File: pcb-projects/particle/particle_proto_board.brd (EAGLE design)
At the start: 60 x 57.8 mm, 37 parts, among them IC1 ATTINY20-SOIC-14S1, IC2 DMC2400UV-SOT563, IC3 DMC2400UV-SOT563

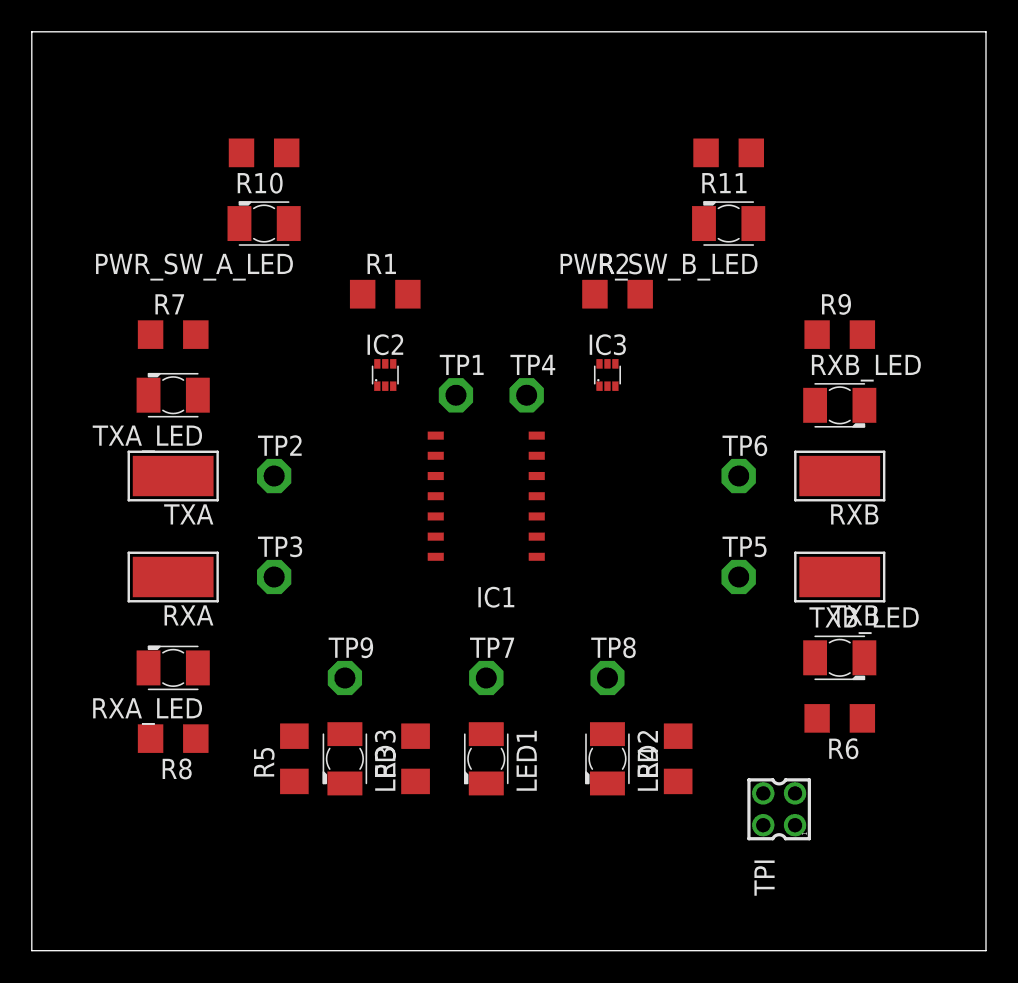
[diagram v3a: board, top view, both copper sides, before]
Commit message: routed bard
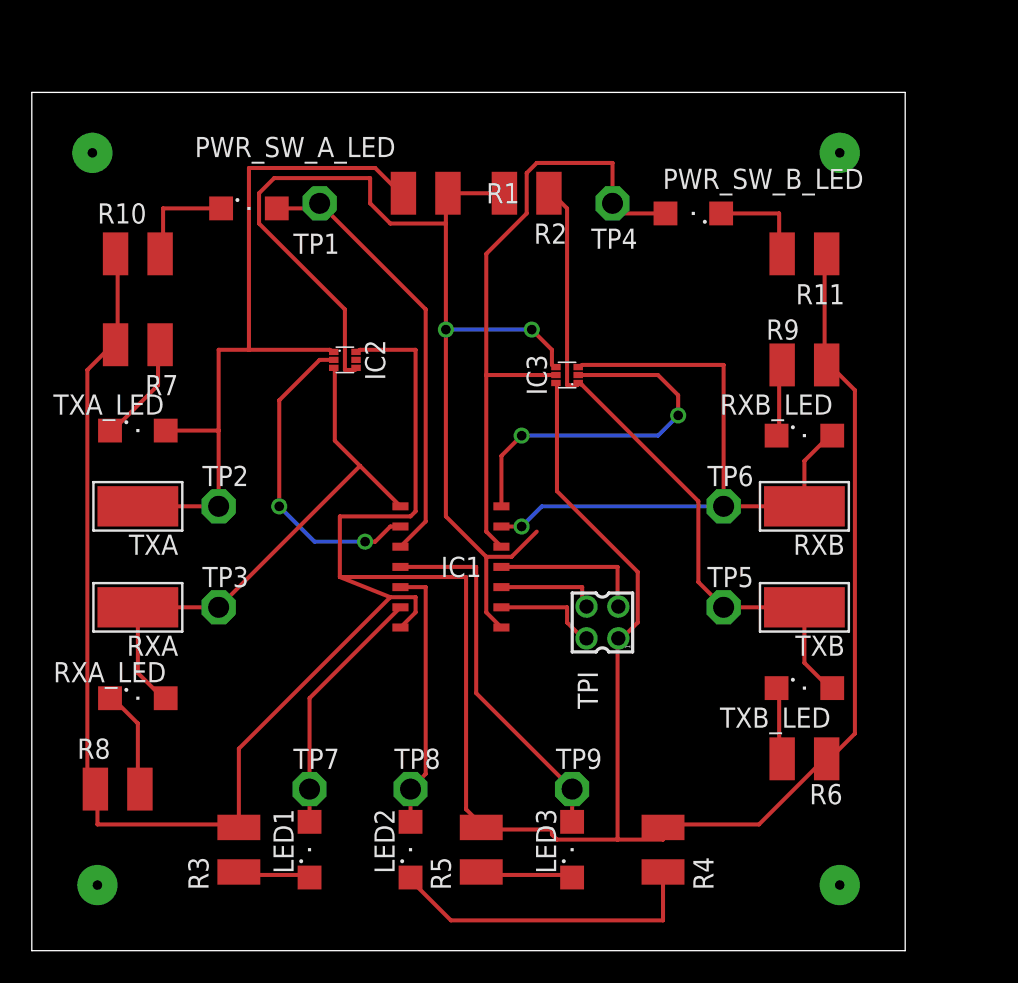
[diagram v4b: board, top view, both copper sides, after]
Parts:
- LED1, LED2, LED3, PWR_SW_A_LED, PWR_SW_B_LED, RXA_LED, RXB_LED, TXA_LED, TXB_LED: device led:KA-3528ASYC -> led:SML1206
- R1, R10, R11, R2, R3, R4, R5, R6, R7, R8, R9: device rcl:R1206 -> rcl:R1210
- moved TPI 16.2 mm to (35.9, 20.6)
- moved TP9 15.9 mm to (34.0, 10.2)
- moved LED3 15.4 mm to (34.0, 6.35), turned to 90 degrees
- moved TP1 14.8 mm to (18.1, 47.0)
- moved TP8 14.2 mm to (23.8, 10.2)
- moved LED2 13.6 mm to (23.8, 6.35), turned to 90 degrees
- moved TP4 13.2 mm to (36.5, 47.0)
- moved TP7 13.1 mm to (17.5, 10.2)
- moved R5 13.1 mm to (28.3, 6.35)
- moved LED1 12.5 mm to (17.5, 6.35), turned to 90 degrees
- moved R3 12.5 mm to (13.0, 6.35)
- moved R10 10.2 mm to (6.67, 43.8), turned to 0 degrees
- moved R2 8.54 mm to (31.1, 47.6), turned to 180 degrees
- moved R11 7.94 mm to (48.6, 43.8)
- moved R1 6.84 mm to (24.8, 47.6)
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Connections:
- net PWR_RX_SW_A: now also IC1.10; no longer IC1.8
- net PWR_RX_SW_B: now also IC1.5; no longer IC1.7
- net PWR_TX_A: now also IC1.9; no longer IC1.10
- net PWR_TX_B: now also IC1.7; no longer IC1.6
- net RX_A: now also IC1.8; no longer IC1.9
- net RX_B: now also IC1.6; no longer IC1.5
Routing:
- net GND: track 0.00 -> 208.9 mm, vias 0 -> 4
- net +5V: track 0.00 -> 73.1 mm, vias 0 -> 2
- net PWR_TX_A_A_A: track 0.00 -> 47.3 mm
- net RX_B: track 0.00 -> 42.9 mm, vias 0 -> 1
- net TXB: track 0.00 -> 42.4 mm
- net PWR_RX_SW_B: track 0.00 -> 41.5 mm
- net RX_A: track 0.00 -> 34.6 mm
- net PWR_RX_SW_A: track 0.00 -> 28.0 mm
- net PWR_TX_B: track 0.00 -> 23.4 mm, vias 0 -> 2
- net N$2: track 0.00 -> 23.3 mm
- net N$6: track 0.00 -> 20.1 mm
- net PWR_TX_A: track 0.00 -> 20.1 mm, vias 0 -> 2
- net N$3: track 0.00 -> 16.7 mm
- net N$1: track 0.00 -> 15.9 mm
- net RESET: track 0.00 -> 9.80 mm
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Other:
- board size 60 x 57.8 mm -> 54.9 x 54 mm

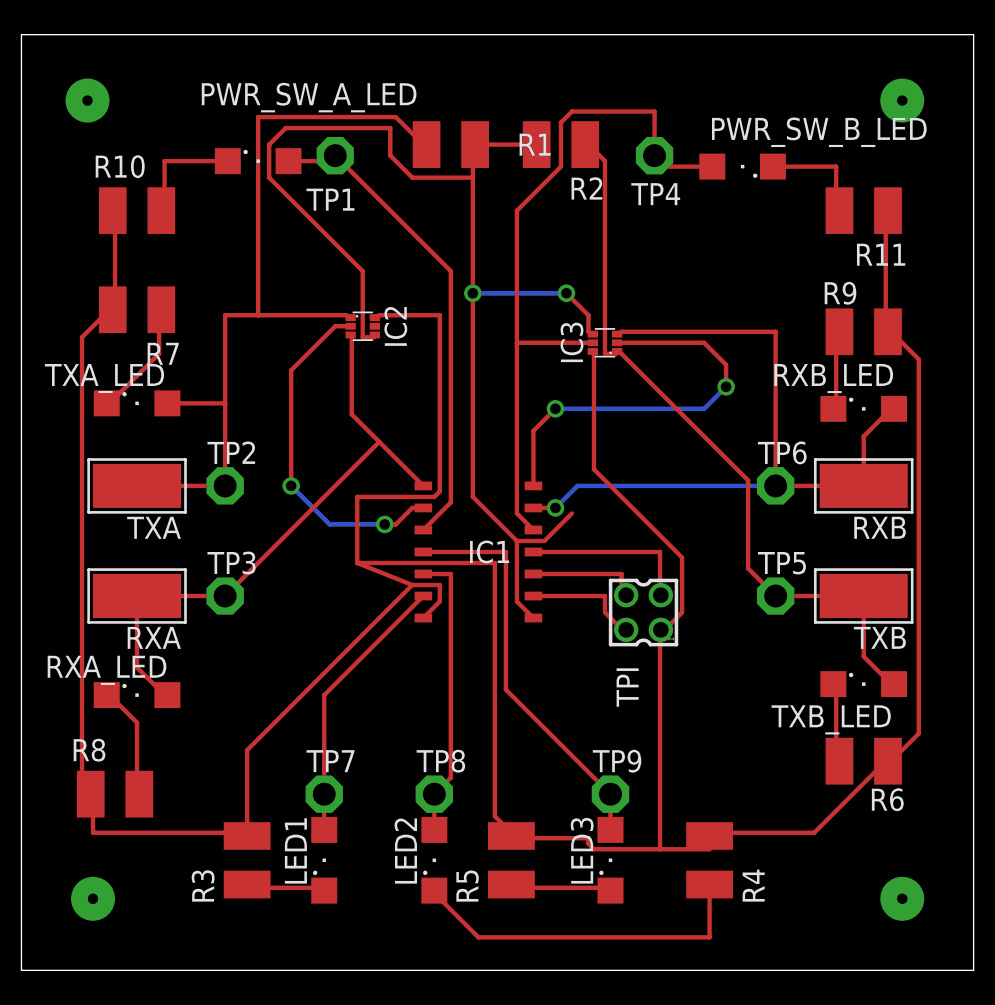
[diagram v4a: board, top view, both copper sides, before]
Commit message: added missing track and vcc/gnd holes
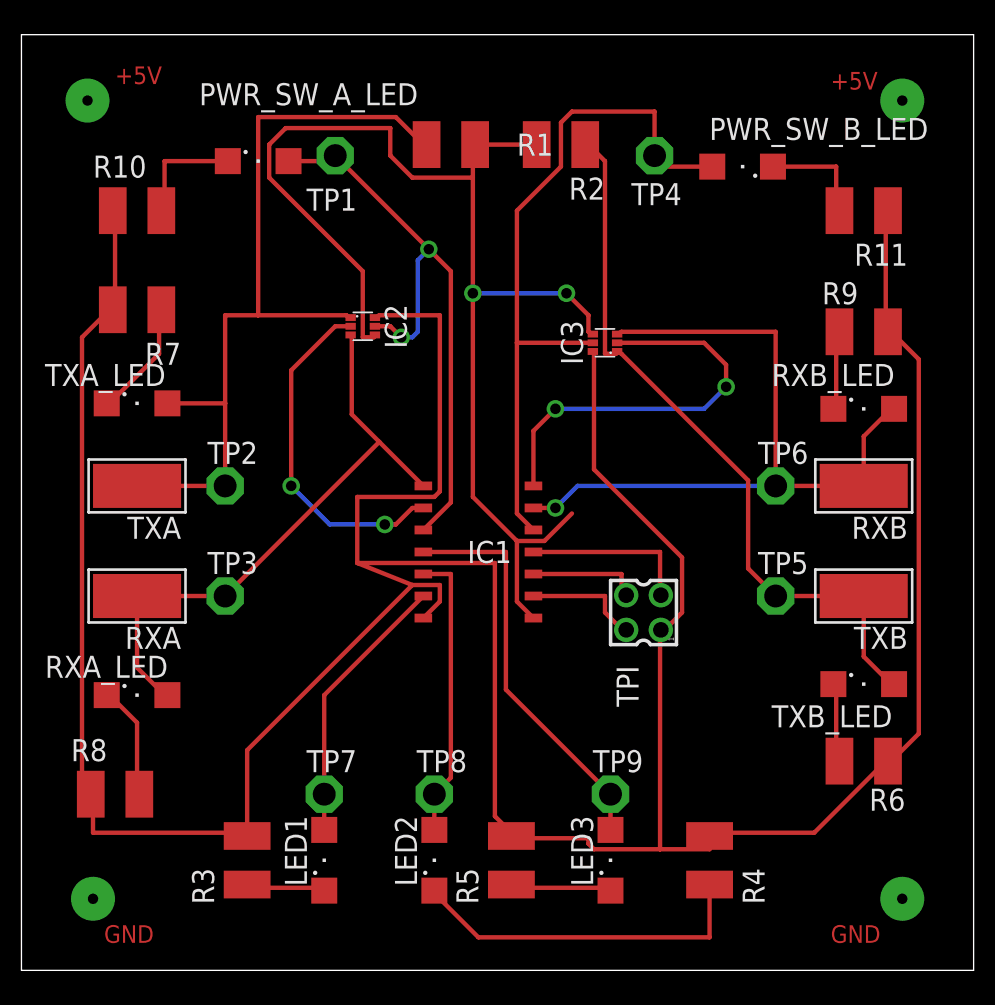
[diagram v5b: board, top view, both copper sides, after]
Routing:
- net PWR_RX_SW_A: track 28.0 -> 35.9 mm, vias 0 -> 2
- net GND: vias 4 -> 2
- net +5V: vias 2 -> 4
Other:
- board text added: "+5V"
- board text added: "GND"
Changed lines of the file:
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@@
 <setting verticaltext="up"/>
 </settings>
-<grid distance="0.3175" unitdist="mm" unit="mm" style="lines" multiple="1" display="no" altdistance="0.025" altunitdist="inch" altunit="inch"/>
+<grid distance="0.0125" unitdist="inch" unit="inch" style="lines" multiple="1" display="no" altdistance="0.025" altunitdist="inch" altunit="inch"/>
 <layers>
 <layer number="1" name="Top" color="4" fill="1" visible="yes" active="yes"/>
@@
 <wire x1="54.915" y1="53.965" x2="0" y2="53.965" width="0" layer="20"/>
 <wire x1="0" y1="53.965" x2="0" y2="0" width="0" layer="20"/>
+<text x="5.3975" y="51.1175" size="1.016" layer="1">+5V</text>
+<text x="46.6725" y="50.8" size="1.016" layer="1">+5V</text>
+<text x="4.7625" y="1.5875" size="1.016" layer="1">GND</text>
+<text x="46.6725" y="1.5875" size="1.016" layer="1">GND</text>
 </plain>
 <attributes>
@@
 <via x="26.035" y="39.0525" extent="1-16" drill="0.6096"/>
 <wire x1="26.035" y1="39.0525" x2="26.035" y2="38.735" width="0.3048" layer="1"/>
+<via x="3.81" y="50.165" extent="1-16" drill="0.6" diameter="2.54"/>
+<via x="50.8" y="50.165" extent="1-16" drill="0.6" diameter="2.54"/>
+<wire x1="29.715" y1="47.625" x2="50.8" y2="50.165" width="0" layer="19" extent="1-1"/>
+<wire x1="3.81" y1="50.165" x2="14.2875" y2="47.625" width="0" layer="19" extent="1-1"/>
 </signal>
 <signal name="GND">
@@
 <wire x1="28.2575" y1="7.9375" x2="28.2575" y2="7.75" width="0.254" layer="1"/>
 <via x="4.1275" y="4.1275" extent="1-16" drill="0.6" diameter="2.54"/>
-<via x="3.81" y="50.165" extent="1-16" drill="0.6" diameter="2.54"/>
 <via x="50.8" y="4.1275" extent="1-16" drill="0.6" diameter="2.54"/>
 <wire x1="45.72" y1="7.9375" x2="50.8" y2="4.1275" width="0" layer="19" extent="1-1"/>
 <wire x1="4.1275" y1="4.1275" x2="4.1275" y2="7.9375" width="0" layer="19" extent="1-1"/>
-<wire x1="3.81" y1="50.165" x2="5.2675" y2="43.815" width="0" layer="19" extent="1-1"/>
-<via x="50.8" y="50.165" extent="1-16" drill="0.6" diameter="2.54"/>
 </signal>
 <signal name="TPI_CLK">
@@
 <wire x1="24.765" y1="26.9875" x2="23.1775" y2="25.4" width="0.254" layer="1"/>
 <wire x1="24.765" y1="40.3225" x2="24.765" y2="26.9875" width="0.254" layer="1"/>
-<wire x1="18.0975" y1="46.99" x2="24.765" y2="40.3225" width="0.254" layer="1"/>
+<wire x1="18.0975" y1="46.99" x2="23.495" y2="41.5925" width="0.254" layer="1"/>
+<wire x1="23.8125" y1="41.275" x2="24.765" y2="40.3225" width="0.254" layer="1"/>
 <wire x1="18.0975" y1="46.6725" x2="15.4025" y2="46.6725" width="0.254" layer="1"/>
 <wire x1="18.0975" y1="46.99" x2="18.0975" y2="46.6725" width="0.254" layer="1"/>
-<wire x1="24.765" y1="40.3225" x2="20.385" y2="37.1475" width="0" layer="19" extent="1-1"/>
+<wire x1="20.385" y1="37.1475" x2="21.2725" y2="37.1475" width="0.254" layer="1"/>
+<wire x1="21.2725" y1="37.1475" x2="21.9075" y2="36.5125" width="0.254" layer="1"/>
+<via x="21.9075" y="36.5125" extent="1-16" drill="0.6"/>
+<wire x1="21.9075" y1="36.5125" x2="22.5425" y2="36.5125" width="0.254" layer="16"/>
+<wire x1="22.5425" y1="36.5125" x2="22.86" y2="36.83" width="0.254" layer="16"/>
+<wire x1="22.86" y1="36.83" x2="22.86" y2="40.9575" width="0.254" layer="16"/>
+<wire x1="22.86" y1="40.9575" x2="23.495" y2="41.5925" width="0.254" layer="16"/>
+<via x="23.495" y="41.5925" extent="1-16" drill="0.6"/>
+<wire x1="23.495" y1="41.5925" x2="23.8125" y2="41.275" width="0.254" layer="1"/>
 </signal>
 <signal name="RX_A" class="1">

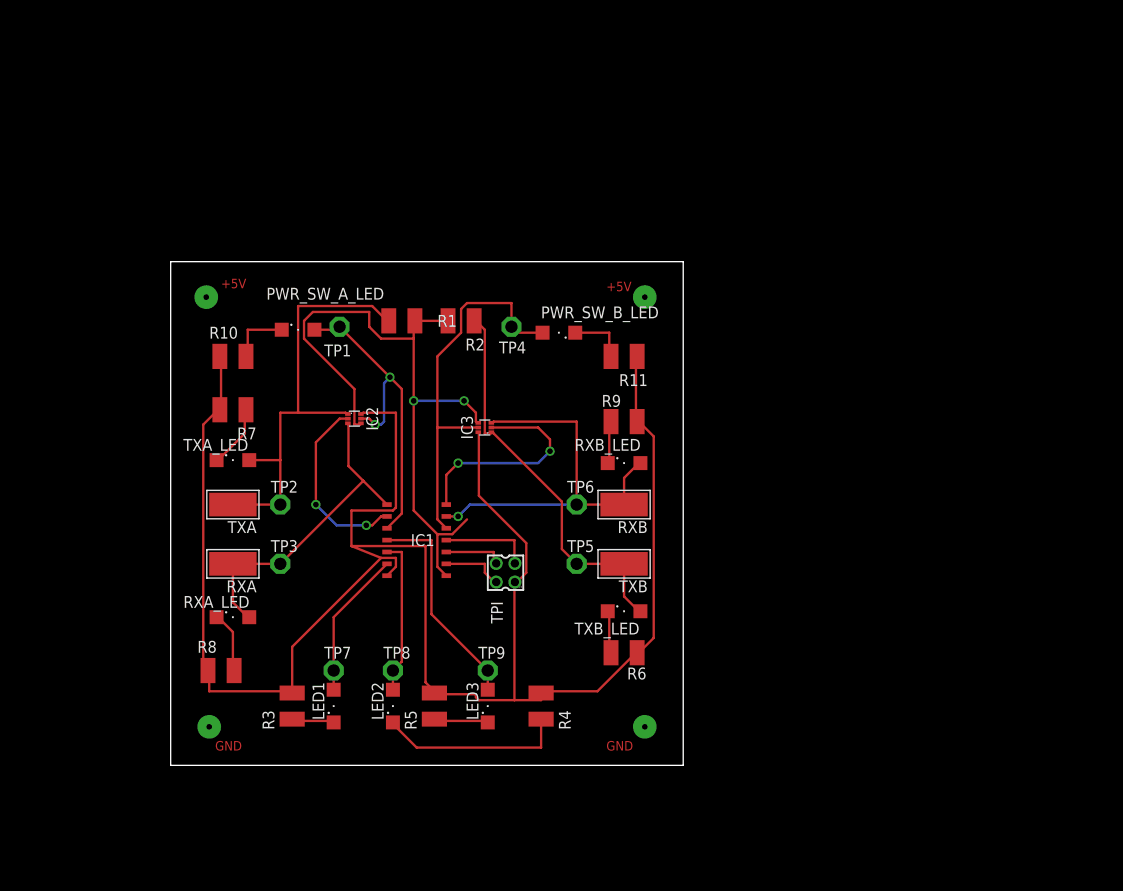
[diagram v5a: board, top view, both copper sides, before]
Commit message: replaced packages/library of attiny20 and dmc2400uv
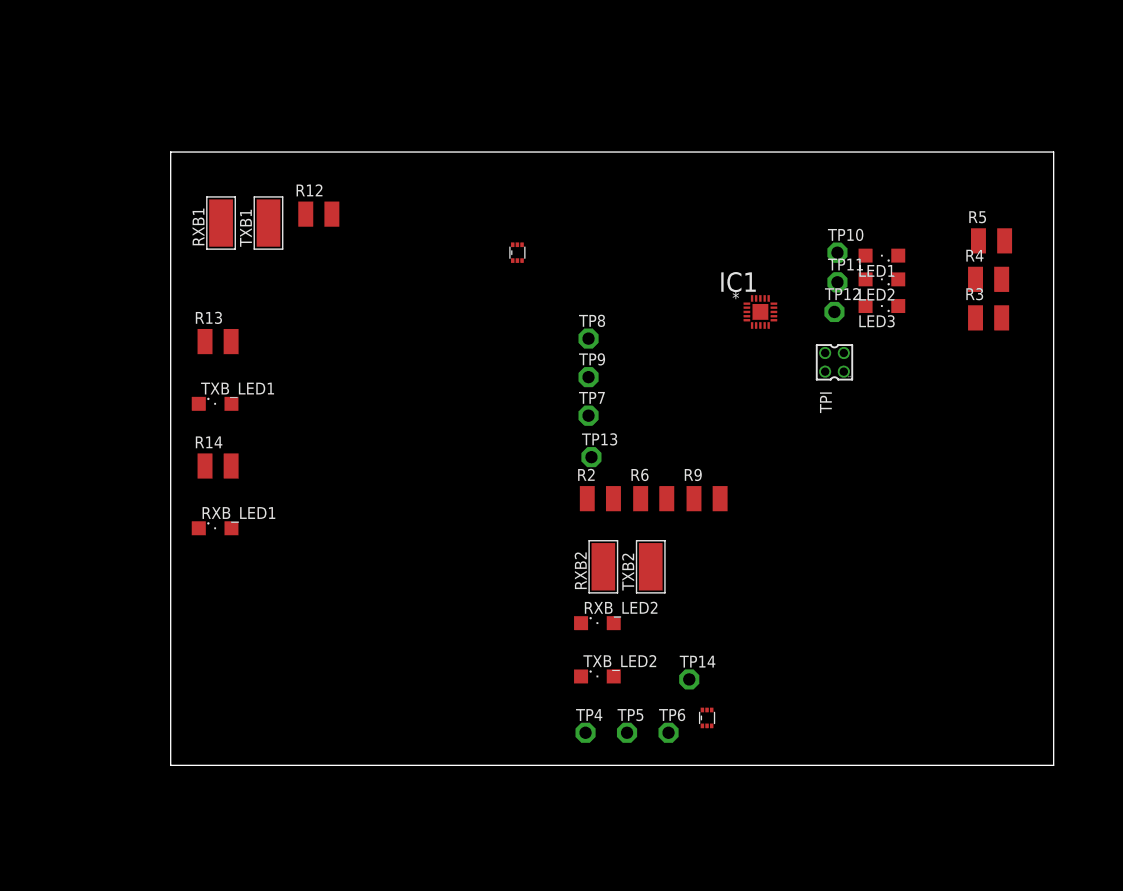
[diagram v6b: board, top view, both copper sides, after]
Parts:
- removed PWR_SW_A_LED, PWR_SW_B_LED, RXA_LED, RXB_LED, TXA_LED, TXB_LED: a, led:SML1206
- removed R1: 1k, rcl:R1210
- removed R10, R11, R7, R8: 470, rcl:R1210
- removed RXA, RXB, TXA, TXB: WIREPADSMD5-2,5, wirepad:5-2,5
- removed TP1, TP2, TP3: TPSPAD1-13, testpad:P1-13
- added R12: 1k, rcl:R1210
- added R13, R14: 470, rcl:R1210
- added RXB1, RXB2, TXB1, TXB2: WIREPADSMD5-2,5, wirepad:5-2,5
- added RXB_LED1, RXB_LED2, TXB_LED1, TXB_LED2: a, led:SML1206
- added TP10, TP11, TP12, TP13, TP14: TPSPAD1-13, testpad:P1-13
- IC1: value ATTINY20-SOIC-14S1 -> ATTINY20-MMH; device ic-attiny20:SOIC14-14S1 -> tiny_particles_MCU:QFN45P300X300X85-21N
- IC2, IC3: value DMC2400UV-SOT563 -> DMC2400V; device dmc2400uv:SOT563 -> diodes:SOT563
- moved R3 85.4 mm to (87.6, 47.9), turned to 0 degrees
- moved R5 77.8 mm to (87.9, 56.2), turned to 0 degrees
- moved LED1 76.0 mm to (76.2, 54.6), turned to 180 degrees
- moved LED2 69.5 mm to (76.2, 52.1), turned to 180 degrees
- moved R4 66.2 mm to (87.6, 52.1), turned to 0 degrees
- moved LED3 60.2 mm to (76.2, 49.2), turned to 180 degrees
- moved IC2 49.6 mm to (57.5, 5.08), turned to 0 degrees
- moved TP4 44.2 mm to (44.5, 3.49)
- moved IC1 44.2 mm to (63.2, 48.6), turned to 0 degrees
- moved TPI 41.8 mm to (71.1, 43.2)
- moved TP8 41.3 mm to (44.8, 45.7)
- moved TP7 38.6 mm to (44.8, 37.5)
- moved TP9 33.2 mm to (44.8, 41.6)
- moved TP6 26.4 mm to (53.3, 3.49)
- moved R2 24.2 mm to (46.0, 28.6), turned to 0 degrees
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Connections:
- removed net +5V: IC1.1, IC2.4, IC3.4, R1.2, R2.2
- removed net N$11: R8.2, RXA_LED.C
- removed net N$12: R9.2, RXB_LED.C
- removed net N$13: PWR_SW_A_LED.C, R10.2
- removed net N$14: PWR_SW_B_LED.C, R11.2
- removed net N$5: R6.1, TXB_LED.C
- removed net N$7: R7.1, TXA_LED.C
- removed net PWR_RX_SW_A: IC1.10, IC2.5, PWR_SW_A_LED.A, TP1.TP
- removed net PWR_RX_SW_B: IC1.5, IC3.5, PWR_SW_B_LED.A, TP4.TP
- removed net PWR_TX_A_A_A: IC2.1, R1.1, TP2.TP, TXA.1, TXA_LED.A
- removed net TXB: IC3.1, R2.1, TP5.TP, TXB.1, TXB_LED.A
- new net N$21: IC1.16, LED1.A, TP10.TP
- new net N$22: IC1.14, LED3.A, TP12.TP
- new net N$23: IC1.15, LED2.A, TP11.TP
- new net N$24: LED1.C, R5.1
- new net N$26: LED3.C, R3.1
- new net N$6: R13.2, TXB_LED1.C
- new net SW_PWR_RX_A: IC1.2, IC2.5, TP5.TP
- new net SW_PWR_RX_B: IC1.5, IC3.5, TP9.TP
- new net VCC: IC1.9, IC2.4, IC3.4, R12.2, R2.2
- net GND: now also IC1.21, IC1.8, IC2.1, IC3.1, R13.1, R14.1, R6.1; no longer IC1.14, IC2.6, IC3.6, R10.1, R11.1, R6.2, R7.2, R8.1
- net N$1: now also IC3.6, R12.1, TXB1.1, TXB_LED1.A; no longer IC1.13, LED1.A
- net N$2: now also IC2.6, R2.1, TP6.TP, TXB2.1, TXB_LED2.A; no longer IC1.11, LED3.A, TP9.TP
- net N$3: now also R6.2, TXB_LED2.C; no longer IC1.12, LED2.A, TP8.TP
- net N$4: now also R9.2, RXB_LED2.C; no longer LED1.C, R3.1
- net N$8: now also R14.2, RXB_LED1.C; no longer LED3.C, R5.1
- net PWR_TX_A: now also IC1.1, TP14.TP; no longer IC1.9
- net PWR_TX_B: now also IC1.4, TP13.TP; no longer IC1.7
- net RESET: now also IC1.13; no longer IC1.4
- net RX_A: now also IC1.17, RXB2.1, RXB_LED2.A, TP4.TP; no longer IC1.8, RXA.1, RXA_LED.A, TP3.TP
- net RX_B: now also IC1.3, RXB1.1, RXB_LED1.A, TP8.TP; no longer IC1.6, RXB.1, RXB_LED.A, TP6.TP
- net TPI_CLK: now also IC1.11; no longer IC1.2
- net TPI_DATA: now also IC1.12; no longer IC1.3
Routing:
- net GND: track 208.9 -> 0.00 mm, vias 2 -> 0
- net +5V: track 73.1 -> 0.00 mm, vias 4 -> 0
- net PWR_TX_A_A_A: track 47.3 -> 0.00 mm
- net RX_B: track 42.9 -> 0.00 mm, vias 1 -> 0
- net TXB: track 42.4 -> 0.00 mm
- net PWR_RX_SW_B: track 41.5 -> 0.00 mm
- net PWR_RX_SW_A: track 35.9 -> 0.00 mm, vias 2 -> 0
- net RX_A: track 34.6 -> 0.00 mm
- net PWR_TX_B: track 23.4 -> 0.00 mm, vias 2 -> 0
- net N$2: track 23.3 -> 0.00 mm
- net N$25: track 20.1 -> 0.00 mm
- net PWR_TX_A: track 20.1 -> 0.00 mm, vias 2 -> 0
- net N$3: track 16.7 -> 0.00 mm
- net N$1: track 15.9 -> 0.00 mm
- net RESET: track 9.80 -> 0.00 mm
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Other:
- board size 54.9 x 54 mm -> 94.6 x 65.7 mm
- board text removed: "+5V"
- board text removed: "GND"
